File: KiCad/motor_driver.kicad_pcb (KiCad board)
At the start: 2 copper layers, 45.7 x 73.7 mm, 17 parts, among them J1 sig_m1, J10 m4, J11 m5, J12 m6, J13 Conn_01x03, J14 power12v, J2 sig_m2, J3 sig_m3, J4 sig_m4, J5 sig_m5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

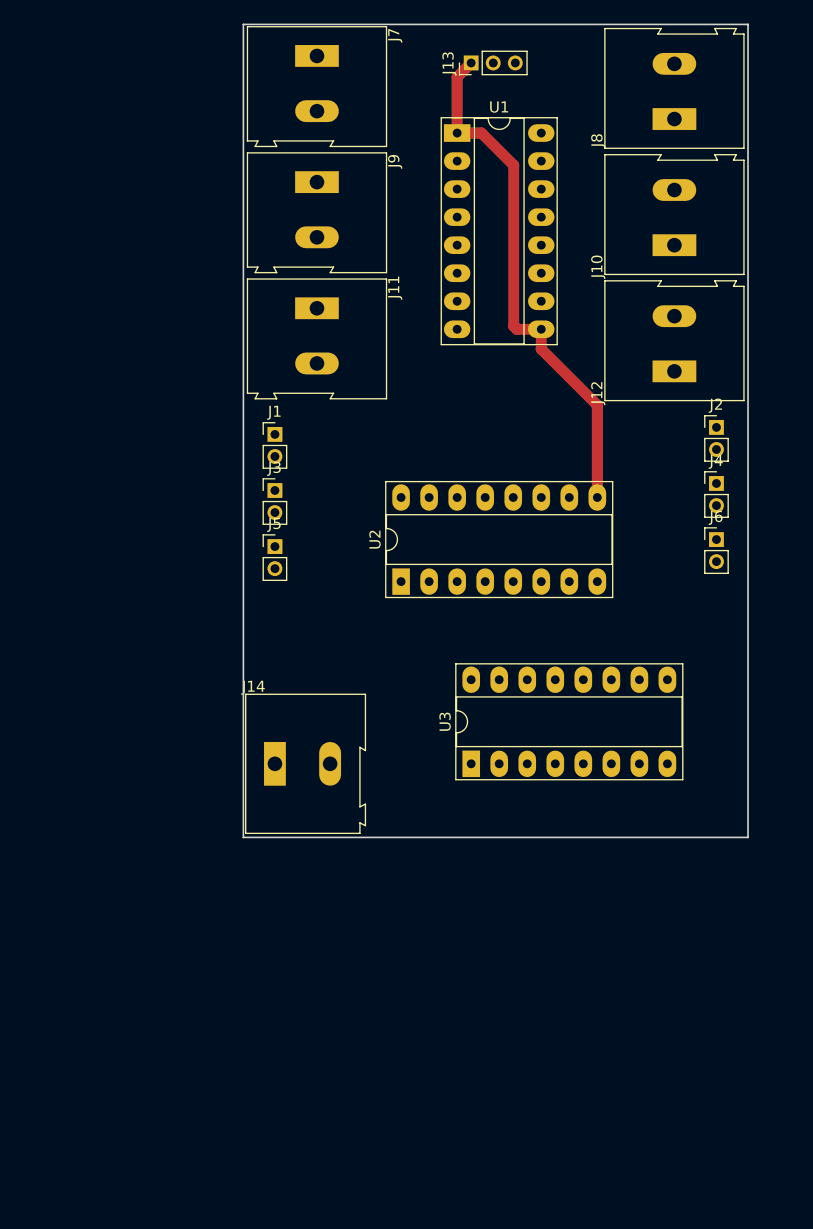
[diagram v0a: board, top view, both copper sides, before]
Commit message: one f*** layer pcb finished, with just 3 bridges
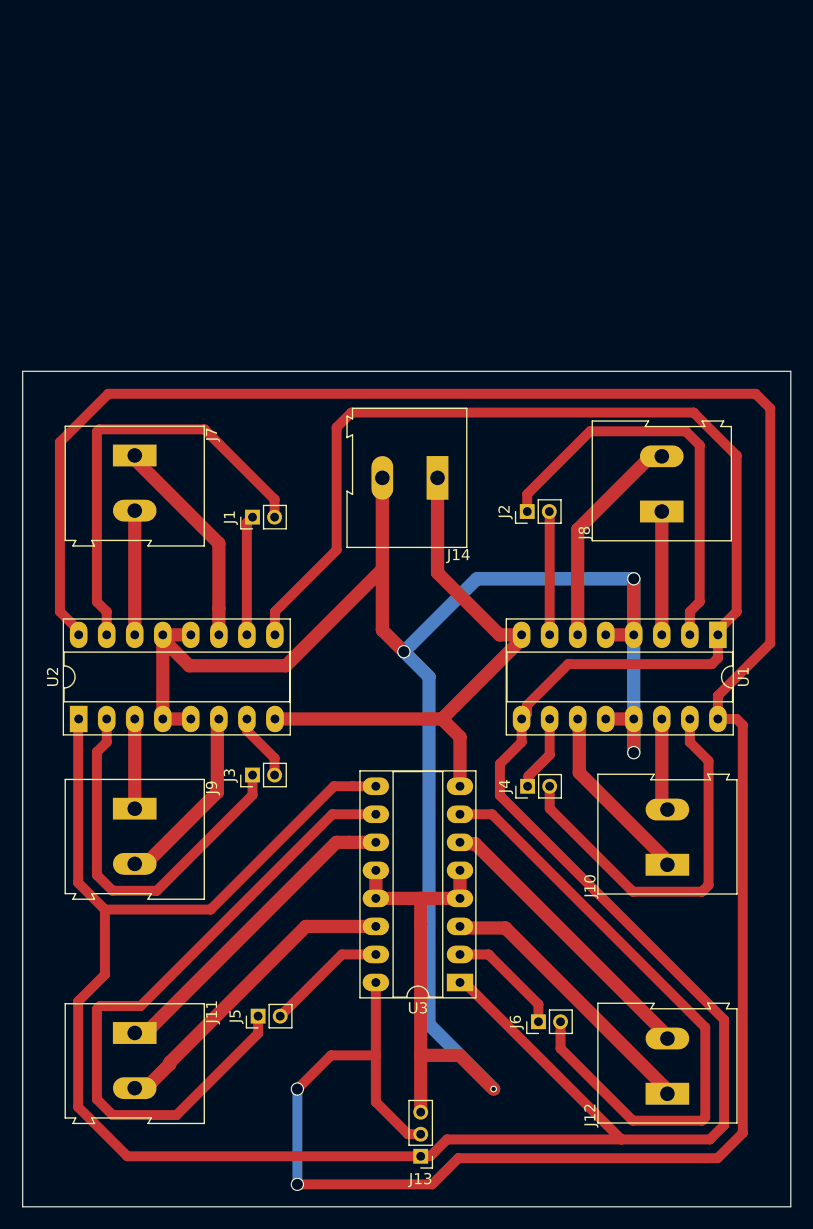
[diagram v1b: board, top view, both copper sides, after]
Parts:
- J1: value sig_m1 -> Conn_01x02
- J2: value sig_m2 -> Conn_01x02
- J3: value sig_m3 -> Conn_01x02
- J4: value sig_m4 -> Conn_01x02
- J5: value sig_m5 -> Conn_01x02
- J6: value sig_m6 -> Conn_01x02
- moved J13 99.2 mm to (89.4, 121.9), turned to 180 degrees
- moved J11 67.7 mm to (63.5, 110.7)
- moved J12 65.5 mm to (111.8, 116.3)
- moved J9 59.1 mm to (63.5, 90.4)
- moved J10 56.1 mm to (111.8, 95.5)
- moved U1 51.2 mm to (116.3, 74.7), turned to 270 degrees
- moved J6 46.6 mm to (100.1, 109.7), turned to 90 degrees
- moved J5 42.6 mm to (74.7, 109.2), turned to 90 degrees
- moved J7 39.8 mm to (63.5, 58.4)
- moved J8 35.6 mm to (111.3, 63.5)
- moved J4 32.3 mm to (99.1, 88.4), turned to 90 degrees
- moved U2 31.8 mm to (58.4, 82.3)
- moved J14 29.8 mm to (90.9, 60.5), turned to 180 degrees
- moved J3 25.9 mm to (74.2, 87.4), turned to 90 degrees
- moved U3 19.8 mm to (93.0, 106.2), turned to 180 degrees
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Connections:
- U1 pad 10: pwm_m2 -> pwm_m4
- U1 pad 11: m2- -> m4+
- U1 pad 14: m2+ -> m4-
- U1 pad 15: dig_m2 -> dig_m4
- U1 pad 2: pwm_m1 -> pwm_m2
- U1 pad 3: m1+ -> m2+
- U1 pad 6: m1- -> m2-
- U1 pad 7: dig_m1 -> dig_m2
- U2 pad 10: pwm_m4 -> pwm_m1
- U2 pad 11: m4- -> m1+
- U2 pad 14: m4+ -> m1-
- U2 pad 15: dig_m4 -> dig_m1
- U2 pad 5: m3- -> GND
- U2 pad 6: (no net) -> m3-
- U3 pad 10: pwm_m6 -> pwm_m5
- U3 pad 11: m6- -> m5+
- U3 pad 14: m6+ -> m5-
- U3 pad 15: dig_m6 -> dig_m5
- U3 pad 2: pwm_m5 -> pwm_m6
- U3 pad 3: m5+ -> m6+
- U3 pad 5: m5- -> GND
- U3 pad 6: (no net) -> m6-
- U3 pad 7: dig_m5 -> dig_m6
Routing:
- net en: track 47.7 -> 293.5 mm
- net ardu5V: track 0.00 -> 229.8 mm, vias 0 -> 2
- net GND: track 0.00 -> 189.3 mm, vias 0 -> 4
- net pwm_m5: track 0.00 -> 60.6 mm
- net dig_m6: track 0.00 -> 56.7 mm
- net supply12V: track 0.00 -> 51.1 mm
- net dig_m1: track 0.00 -> 39.2 mm
- net pwm_m2: track 0.00 -> 37.6 mm
- net dig_m4: track 0.00 -> 35.5 mm
- net pwm_m3: track 0.00 -> 34.6 mm
- net m5+: track 0.00 -> 29.0 mm
- net m5-: track 0.00 -> 28.0 mm
- net m6-: track 0.00 -> 26.3 mm
- net m6+: track 0.00 -> 25.3 mm
- net m2-: track 0.00 -> 19.9 mm
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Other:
- board size 45.7 x 73.7 mm -> 69.6 x 75.7 mm
- net class classic: trace_width 1 -> 0.9; via_dia 1 -> 1.2; via_drill 0.5 -> 1
- net class high_current added: clearance 1, trace_width 1.2, via_dia 1.2, via_drill 1
- rule pad_to_mask_clearance: 0.2 -> 0
